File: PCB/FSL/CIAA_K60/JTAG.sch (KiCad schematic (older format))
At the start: 36 parts, among them J1302 JTAG DEBUG USB, J1303 JTAG DIRECTO, U1301 74HC244, U1302 FT2232H, U1303 93C56, U1304 PRTR5V0U2X, X1301 12Mhz

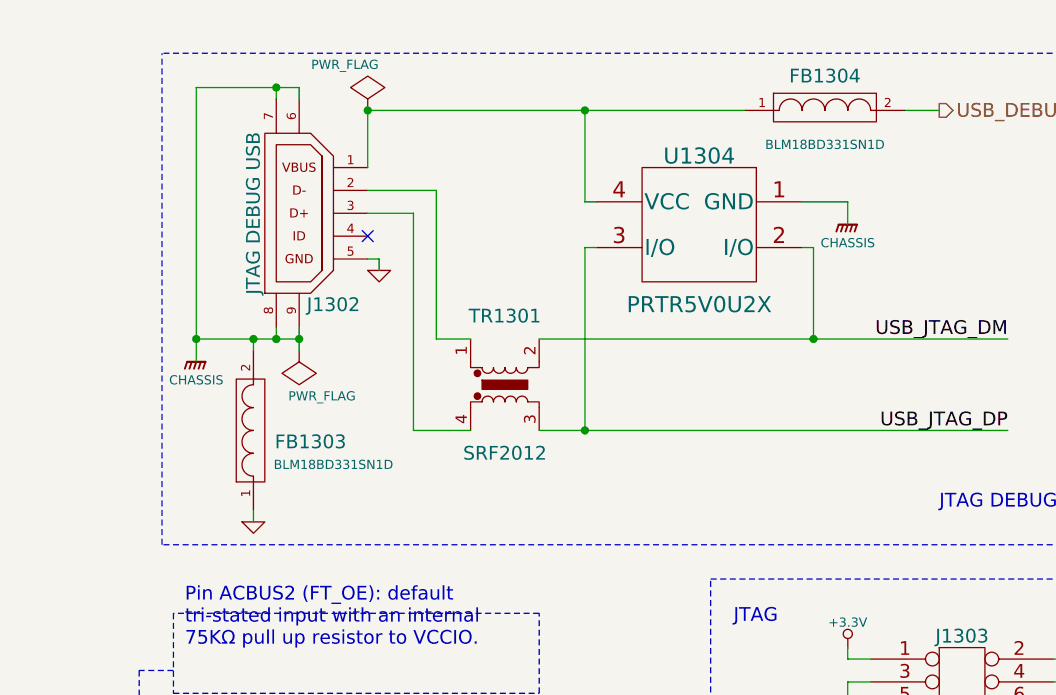
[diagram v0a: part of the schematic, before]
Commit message: Actualizacion de esquematicos. Circuito impreso y modelos 3D
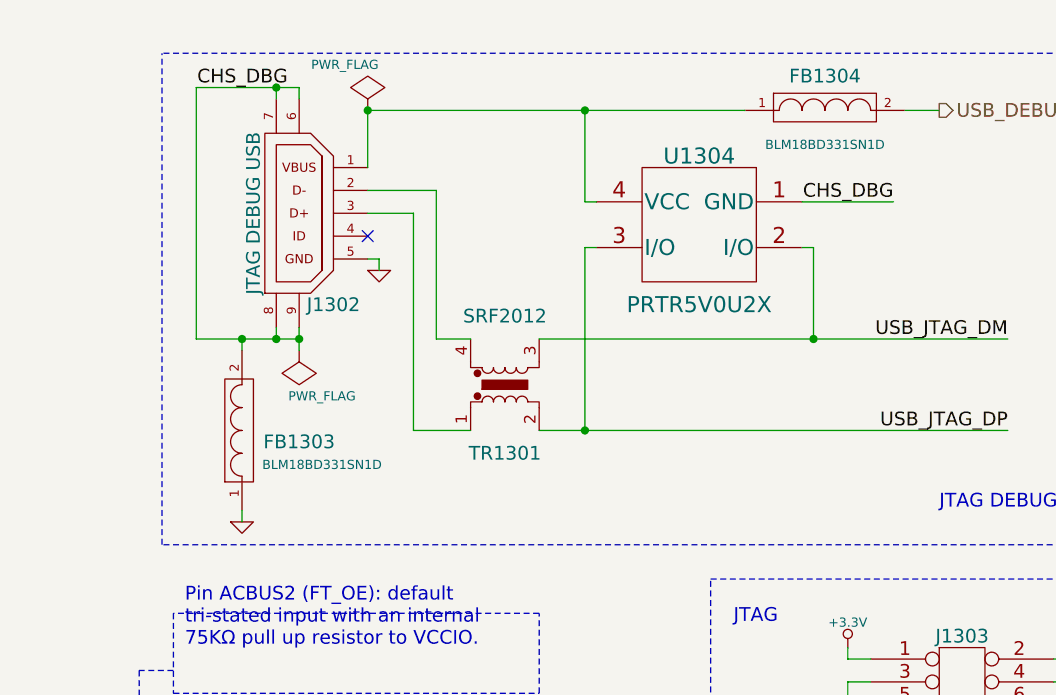
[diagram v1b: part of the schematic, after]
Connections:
- net labels added: CHS_DBG
- net labels removed: CHASSIS
- wire segments 172 -> 171
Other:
- moved on the sheet: FB1303

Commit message: Actualizacion de Licencia y avances
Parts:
- added C1310: 4,7uF, c_1206POL, symbol CAPAPOL
- added C1319: 100nF, c_0603, symbol C
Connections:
- wire segments 171 -> 177

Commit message: - Corregido PCB, según revisiones en doc/revisiones - Actualizado documentación - Modificados 3D para que se vean bien en Freecad
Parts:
- removed C1304: 27pF, c_0603, symbol C
- removed X1301: 12Mhz, FA238V-XTAL, symbol CRYSTAL_4PIN_MINI_GND
- added R1302: 24,9 1%, r_0603, symbol R
- added U1305: SI501, SI501_C, symbol OSCILADOR
- C1301: value 27pF -> 100nF; Descripcion CAP CER 27pF 50V 5% NP0 0603 -> CAP CER 0.1UF 16V 10% X7R; Digikey/Mouser 399-1054-1-ND -> 399-1096-1-ND; Fabricante KEMET -> Kemet; Nro. parte C0603C270J5GACTU -> C0603C104K4RACTU
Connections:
- net labels removed: FT_XTIN, FT_XTOUT
- wire segments 177 -> 175
- no-connect marks 31 -> 32
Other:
- note added: "OSC. 12MHz"
- moved on the sheet: C1303, C1305, C1306, C1307, C1308, C1309, C1311, C1312, C1313, C1314, C1315, C1316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

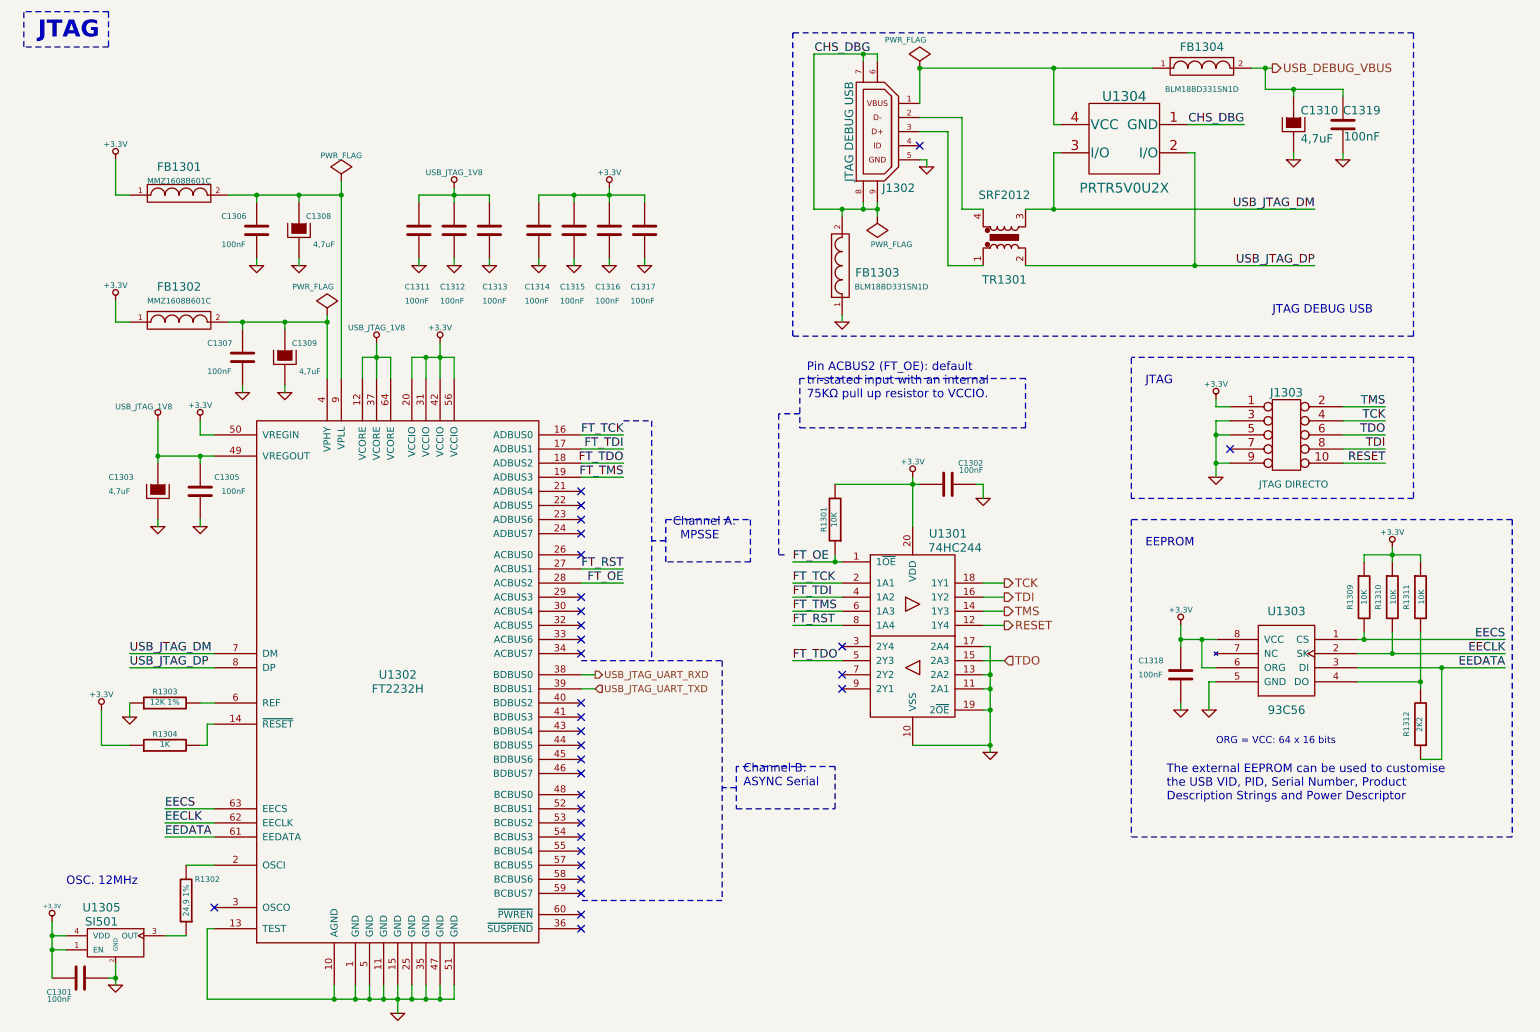
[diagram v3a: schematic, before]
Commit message: CIAA-FSL Versión CEIBO 1.1 - Resumen de cambios en FSL/CIAA_K60/doc/modificaciones - Agregado info de puesta en marcha CEIBO 1.0 - Agregado info de fabricación de la CEIBO 1.0
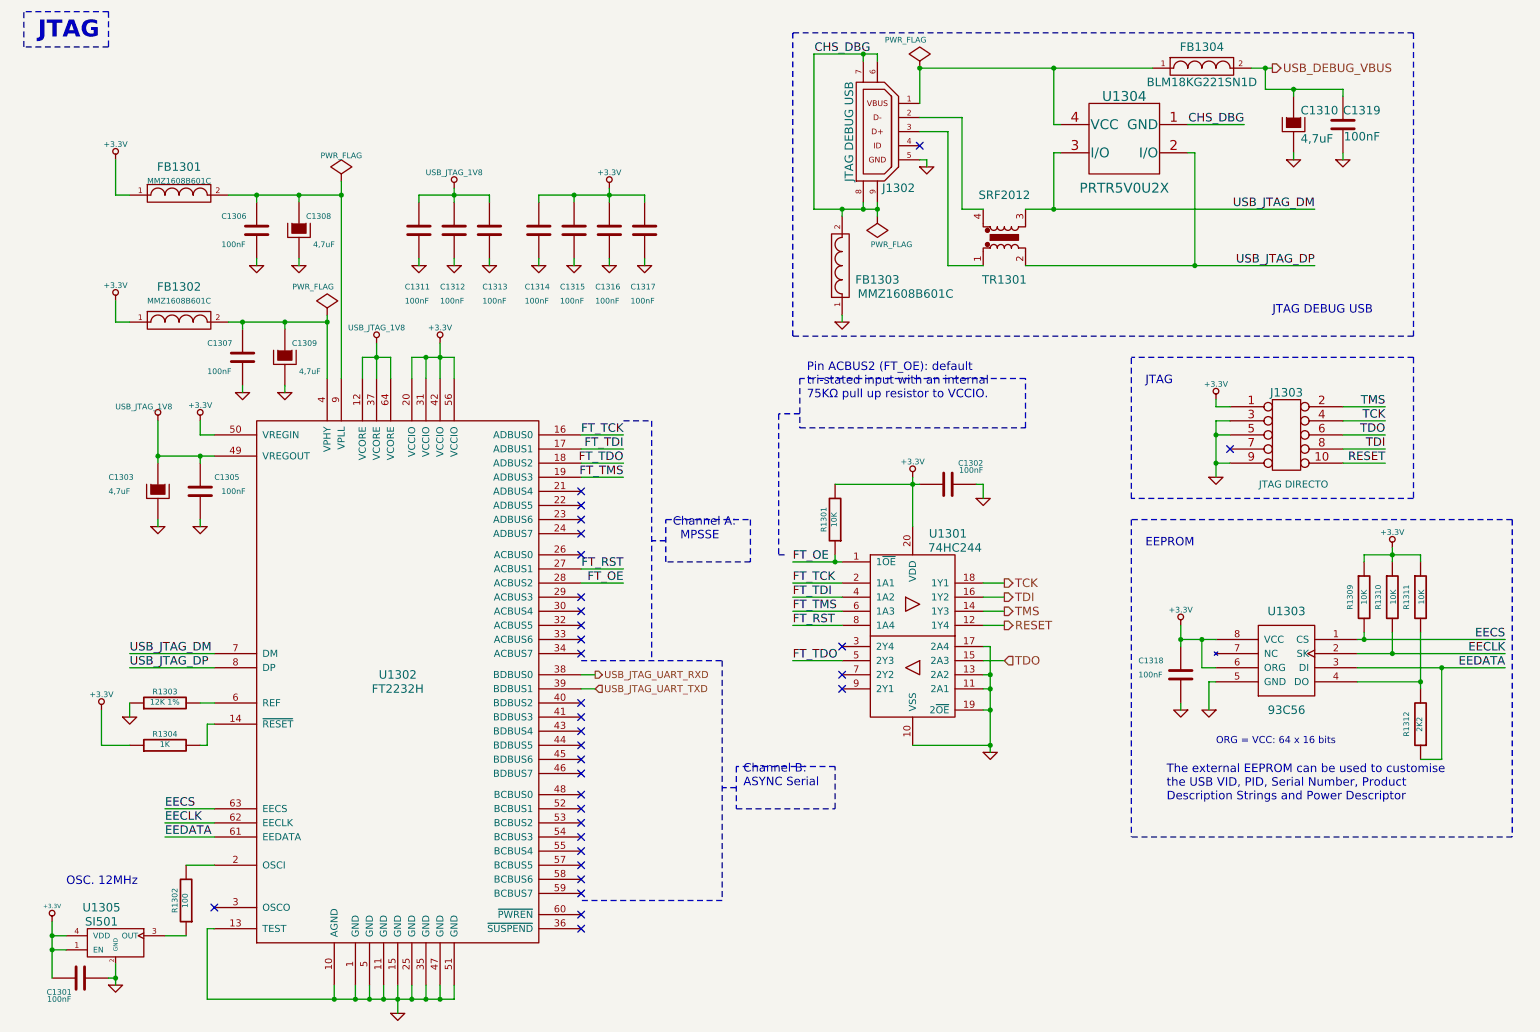
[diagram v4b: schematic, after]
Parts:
- FB1303: value BLM18BD331SN1D -> MMZ1608B601C; Descripcion FERRITE CHIP 330 OHM 200mA 0603 -> FERRITE CHIP 600 OHM 500MA 0603; Digikey/Mouser 490-5251-1-ND -> 445-2166-1-ND; Fabricante MURATA -> TDK; Nro. parte BLM18BD331SN1D -> MMZ1608B601C; Path datasheet ../datasheets/passive/Ferrite/L0110S0100BLM18B.pdf -> ../datasheets/passive/Ferrite/E9412_MMZ.pdf
- FB1304: value BLM18BD331SN1D -> BLM18KG221SN1D; Descripcion FERRITE CHIP 330 OHM 200mA 0603 -> FERRITE CHIP 220 OHM 2200MA 0603; Digikey/Mouser 490-5251-1-ND -> 490-5255-1-ND; Nro. parte BLM18BD331SN1D -> BLM18KG221SN1D; Path datasheet ../datasheets/passive/Ferrite/L0110S0100BLM18B.pdf -> ../datasheets/passive/Ferrite/L0110S0100BLM18K.pdf
- R1302: value 24,9 1% -> 100; Descripcion RES 24.9 OHM 1/10W 1% 0603 SMD -> RES 100 OHM 1/10W 5% 0603 SMD; Digikey/Mouser 311-24.9HRCT-ND -> 311-100GRCT-ND; Fabricante Yageo -> YAGEO; Nro. parte RC0603FR-0724R9L -> RC0603JR-07100RL

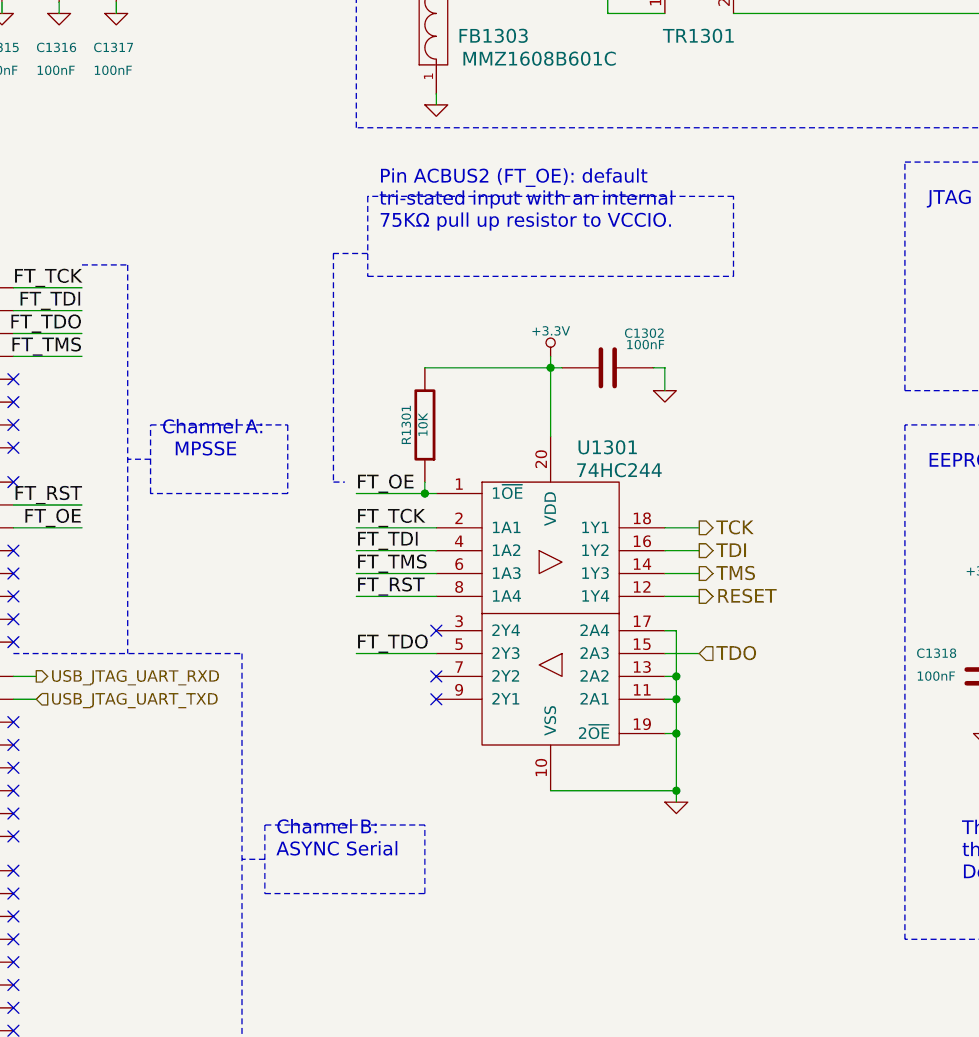
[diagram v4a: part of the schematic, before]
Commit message: Sch files adapted to new eeschema. Fixing some text locations.
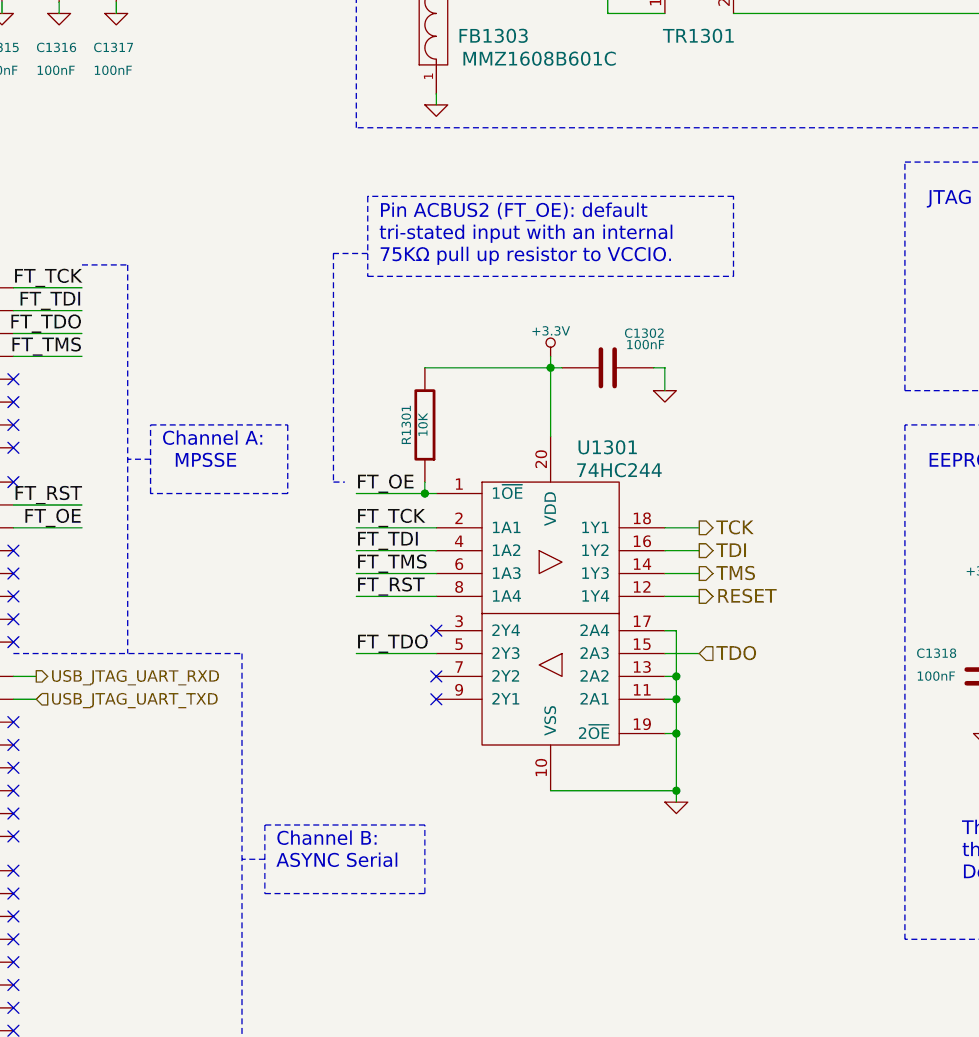
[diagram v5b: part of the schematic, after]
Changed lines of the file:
@@
 EESchema Schematic File Version 2
 LIBS:CIAAK60LIB
-EELAYER 27 0
+LIBS:CIAA_K60-cache
+EELAYER 25 0
 EELAYER END
 $Descr A4 11693 8268
@@
 	1    0    0    -1
 $EndComp
-Text Notes 5150 4300 0    60   ~ 0
+Text Notes 5150 4350 0    60   ~ 0
 Channel A:\n  MPSSE
-Text Notes 5650 6050 0    60   ~ 0
+Text Notes 5650 6100 0    60   ~ 0
  Channel B: \nASYNC Serial
 $Comp
@@
 	1    0    0    -1
 $EndComp
-Text Notes 6100 3300 0    60   ~ 0
+Text Notes 6100 3450 0    60   ~ 0
 Pin ACBUS2 (FT_OE): default\ntri-stated input with an internal\n75KΩ pull up resistor to VCCIO.\n
 NoConn ~ 6350 5250

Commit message: Renaming symbol field-names in .sch files for KiCost integration.
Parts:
- C1301: Desc (none) -> CAP CER 0.1UF 16V 10% X7R; Descripcion CAP CER 0.1UF 16V 10% X7R -> (none); Digikey# (none) -> 399-1096-1-ND; Digikey/Mouser 399-1096-1-ND -> (none); Fabricante Kemet -> (none); Manf (none) -> Kemet; Manf# (none) -> C0603C104K4RACTU; Nro. parte C0603C104K4RACTU -> (none)
- C1302, C1305, C1306, C1307, C1311, C1312, C1313, C1314, C1315, C1316, C1317, C1318: Desc (none) -> CAP CER 0,1UF 16V 10% X7R; Descripcion CAP CER 0,1UF 16V 10% X7R -> (none); Digikey# (none) -> 399-1096-1-ND; Digikey/Mouser 399-1096-1-ND -> (none); Fabricante KEMET -> (none); Manf (none) -> Kemet; Manf# (none) -> C0603C104K4RACTU; Nro. parte C0603C104K4RACTU -> (none)
- C1303, C1308, C1309: Desc (none) -> CAP TANT 4,7UF 6,3V 10% 1206; Descripcion CAP TANT 4,7UF 6,3V 10% 1206 -> (none); Digikey# (none) -> 399-9717-1-ND; Digikey/Mouser 399-9717-1-ND -> (none); Fabricante KEMET -> (none); Manf (none) -> Kemet; Manf# (none) -> T491A475K006AT; Nro. parte T491A475K006AT -> (none)
- C1310: Desc (none) -> CAP TANT 4,7uF 6,3V 10% 1206; Descripcion CAP TANT 4,7uF 6,3V 10% 1206 -> (none); Digikey# (none) -> 399-9717-1-ND; Digikey/Mouser 399-9717-1-ND -> (none); Fabricante KEMET -> (none); Manf (none) -> Kemet; Manf# (none) -> T491A475K006AT; Nro. parte T491A475K006AT -> (none)
- C1319: Desc (none) -> CAP CER 0,1UF 16V X7R 10% 0603; Descripcion CAP CER 0,1UF 16V X7R 10% 0603 -> (none); Digikey# (none) -> 399-1096-1-ND; Digikey/Mouser 399-1096-1-ND -> (none); Fabricante KEMET -> (none); Manf (none) -> Kemet; Manf# (none) -> C0603C104K4RACTU; Nro. parte C0603C104K4RACTU -> (none)
- FB1301, FB1302, FB1303: Desc (none) -> FERRITE CHIP 600 OHM 500MA 0603; Descripcion FERRITE CHIP 600 OHM 500MA 0603 -> (none); Digikey# (none) -> 445-2166-1-ND; Digikey/Mouser 445-2166-1-ND -> (none); Fabricante TDK -> (none); Manf (none) -> TDK; Manf# (none) -> MMZ1608B601C; Nro. parte MMZ1608B601C -> (none)
- FB1304: Desc (none) -> FERRITE CHIP 220 OHM 2200MA 0603; Descripcion FERRITE CHIP 220 OHM 2200MA 0603 -> (none); Digikey# (none) -> 490-5255-1-ND; Digikey/Mouser 490-5255-1-ND -> (none); Fabricante MURATA -> (none); Manf (none) -> MURATA; Manf# (none) -> BLM18KG221SN1D; Nro. parte BLM18KG221SN1D -> (none)
- J1302: Desc (none) -> CONNECTOR RECEPTACLE MICRO USB B SMD; Descripcion CONNECTOR RECEPTACLE MICRO USB B SMD -> (none); Digikey# (none) -> H11634CT-ND; Digikey/Mouser H11634CT-ND -> (none); Fabricante HIROSE ELECTRIC -> (none); Manf (none) -> HIROSE ELECTRIC; Manf# (none) -> ZX62-B-5PA(11); Nro. parte ZX62-B-5PA(11) -> (none)
- J1303: Desc (none) -> CONECTOR HDR 1,27MM SMD AU 10POS; Descripcion CONECTOR HDR 1,27MM SMD AU 10POS -> (none); Digikey# (none) -> 952-1389-ND; Digikey/Mouser 952-1389-ND -> (none); Fabricante HARWIN -> (none); Manf (none) -> HARWIN; Manf# (none) -> M50-3600542; Nro. parte M50-3600542 -> (none)
- R1301, R1309, R1310, R1311: Desc (none) -> RES 10K 1/10W 5% 0603 SMD; Descripcion RES 10K 1/10W 5% 0603 SMD -> (none); Digikey# (none) -> 311-10KGRCT-ND; Digikey/Mouser 311-10KGRCT-ND -> (none); Fabricante YAGEO -> (none); Manf (none) -> Yageo; Manf# (none) -> RC0603JR-0710KL; Nro. parte RC0603JR-0710KL -> (none)
- R1302: Desc (none) -> RES 100 OHM 1/10W 5% 0603 SMD; Descripcion RES 100 OHM 1/10W 5% 0603 SMD -> (none); Digikey# (none) -> 311-100GRCT-ND; Digikey/Mouser 311-100GRCT-ND -> (none); Fabricante YAGEO -> (none); Manf (none) -> Yageo; Manf# (none) -> RC0603JR-07100RL; Nro. parte RC0603JR-07100RL -> (none)
- R1303: Desc (none) -> RES 12.0K OHM 1/10W 1% 0603 SMD; Descripcion RES 12.0K OHM 1/10W 1% 0603 SMD -> (none); Digikey# (none) -> 311-12.0KHRCT-ND; Digikey/Mouser 311-12.0KHRCT-ND -> (none); Fabricante Yageo -> (none); Manf (none) -> Yageo; Manf# (none) -> RC0603FR-0712KL; Nro. parte RC0603FR-0712KL -> (none)
- R1304: Desc (none) -> RES 1.0K OHM 1/10W 5% 0603 SMD; Descripcion RES 1.0K OHM 1/10W 5% 0603 SMD -> (none); Digikey# (none) -> 311-1.0KGRCT-ND; Digikey/Mouser 311-1.0KGRCT-ND -> (none); Fabricante Yageo -> (none); Manf (none) -> Yageo; Manf# (none) -> RC0603JR-071KL; Nro. parte RC0603JR-071KL -> (none)
- R1312: Desc (none) -> RES 2.2K OHM 1/10W 5% 0603 SMD; Descripcion RES 2.2K OHM 1/10W 5% 0603 SMD -> (none); Digikey# (none) -> 311-2.2KGRCT-ND; Digikey/Mouser 311-2.2KGRCT-ND -> (none); Fabricante Yageo -> (none); Manf (none) -> Yageo; Manf# (none) -> RC0603JR-072K2L; Nro. parte RC0603JR-072K2L -> (none)
- TR1301: Desc (none) -> INDUCTOR COMMON MODE 90 OHM SMD; Descripcion INDUCTOR COMMON MODE 90 OHM SMD -> (none); Digikey# (none) -> SRF2012-900YCT-ND; Digikey/Mouser SRF2012-900YCT-ND -> (none); Fabricante BOURNS -> (none); Manf (none) -> BOURNS; Manf# (none) -> SRF2012-900Y; Nro. parte SRF2012-900Y -> (none)
- U1301: Desc (none) -> IC BUFF/DVR TRI-ST DUAL 20TSSOP; Descripcion IC BUFF/DVR TRI-ST DUAL 20TSSOP -> (none); Digikey# (none) -> 568-8285-5-ND; Digikey/Mouser 568-8285-5-ND -> (none); Fabricante NXP -> (none); Manf (none) -> NXP; Manf# (none) -> 74HC244PW,112; Nro. parte 74HC244PW,112 -> (none)
- U1302: Desc (none) -> IC FT2232H DUAL HIGH SPEED USB TO MULTIPURPOSE UART/FIFO; Descripcion IC FT2232H DUAL HIGH SPEED USB TO MULTIPURPOSE UART/FIFO -> (none); Digikey# (none) -> 768-1024-1-ND; Digikey/Mouser 768-1024-1-ND -> (none); Fabricante FTDI CHIP -> (none); Manf (none) -> FTDI CHIP; Manf# (none) -> FT2232HL; Nro. parte FT2232HL -> (none)
- U1303: Desc (none) -> IC EEPROM 1KBIT 2MHZ 8SOIC; Descripcion IC EEPROM 1KBIT 2MHZ 8SOIC -> (none); Digikey# (none) -> AT93C46DN-SH-B-ND; Digikey/Mouser AT93C46DN-SH-B-ND -> (none); Fabricante ATMEL -> (none); Manf (none) -> ATMEL; Manf# (none) -> AT93C46DN-SH-B; Nro. parte AT93C46DN-SH-B -> (none)
- U1304: Desc (none) -> IC TVS DIODE 2 CHANNEL 10V CLAMP SOT1434; Descripcion IC TVS DIODE 2 CHANNEL 10V CLAMP SOT1434 -> (none); Digikey# (none) -> 568-4140-1-ND; Digikey/Mouser 568-4140-1-ND -> (none); Fabricante NXP -> (none); Manf (none) -> NXP; Manf# (none) -> PRTR5V0U2X,215; Nro. parte PRTR5V0U2X,215 -> (none)
- U1305: Desc (none) -> OSC MEMS 12.000MHZ CMOS SMD; Descripcion OSC MEMS 12.000MHZ CMOS SMD -> (none); Digikey# (none) -> 336-2889-ND; Digikey/Mouser 336-2889-ND -> (none); Fabricante Silicon Laboratories -> (none); Manf (none) -> Silicon Laboratories; Manf# (none) -> 501HCA12M0000CAG; Nro. parte 501HCA12M0000CAG -> (none)
